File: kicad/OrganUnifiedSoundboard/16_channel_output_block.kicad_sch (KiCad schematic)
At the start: 4 parts

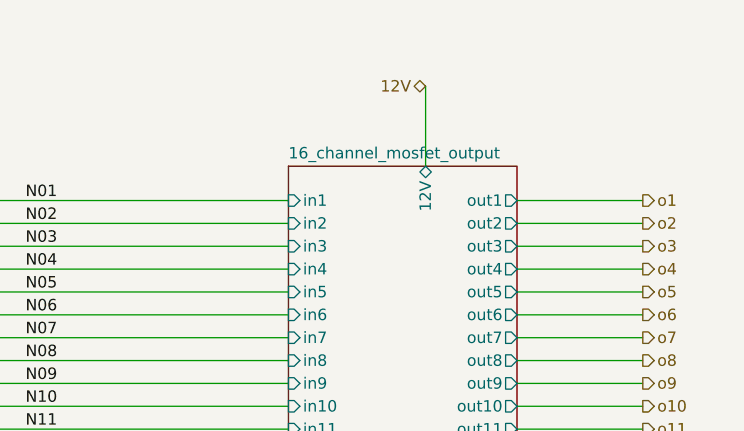
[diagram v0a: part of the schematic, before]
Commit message: Finalized unified soundboard driver for production, adding some models
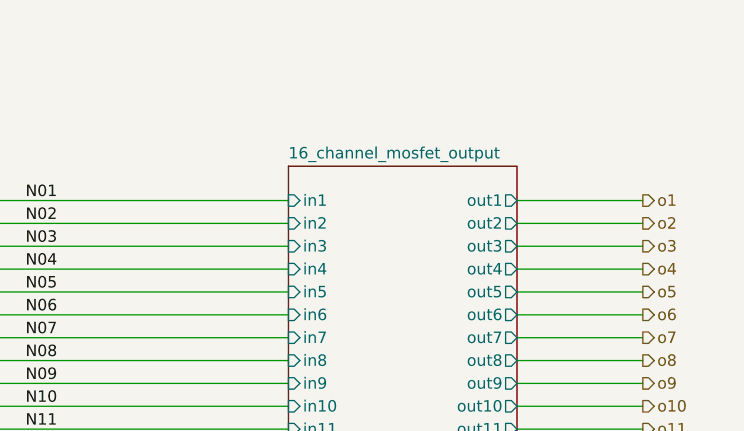
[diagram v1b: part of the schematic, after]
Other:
- sheet 16_channel_mosfet_output ports: added none; removed 12V
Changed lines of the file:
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@@
-	(wire
-		(pts
-			(xy 127 22.86) (xy 127 31.75)
-		)
-		(stroke
-			(width 0)
-			(type default)
-		)
-	)
 	(wire
 		(pts
@@
 		(shape input)
 		(at 41.91 96.52 180)
-		(effects
-			(font
-				(size 1.27 1.27)
-			)
-			(justify right)
-		)
-	)
-	(hierarchical_label "12V"
-		(shape bidirectional)
-		(at 127 22.86 180)
 		(effects
 			(font
@@
 			)
 		)
-		(pin "12V" bidirectional
-			(at 127 31.75 90)
-			(effects
-				(font
-					(size 1.27 1.27)
-				)
-				(justify right)
-			)
-		)
